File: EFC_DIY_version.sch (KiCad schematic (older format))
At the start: 36 parts, among them J1 Screw_Terminal_01x05, Q1 MJE13005G, Q2 2N3906, Q3 2N3904, U1 NE556

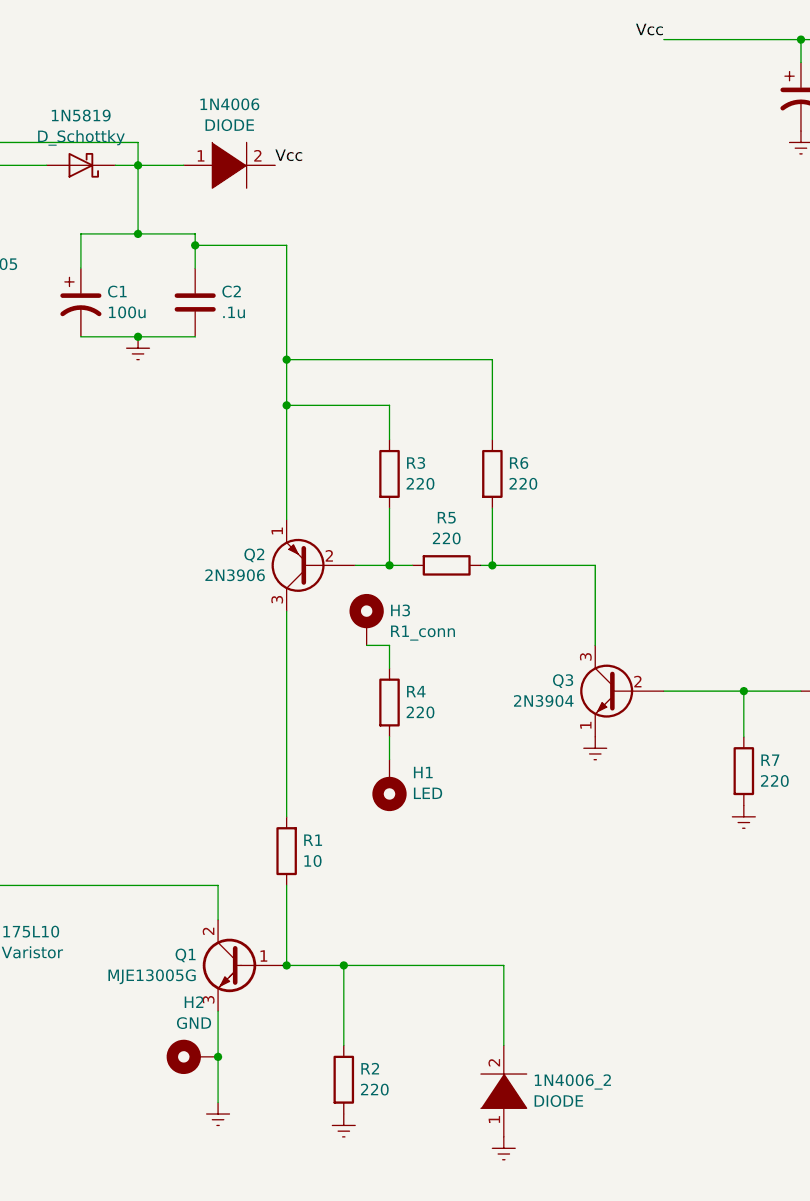
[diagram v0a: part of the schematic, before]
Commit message: Corrected Diode polarity
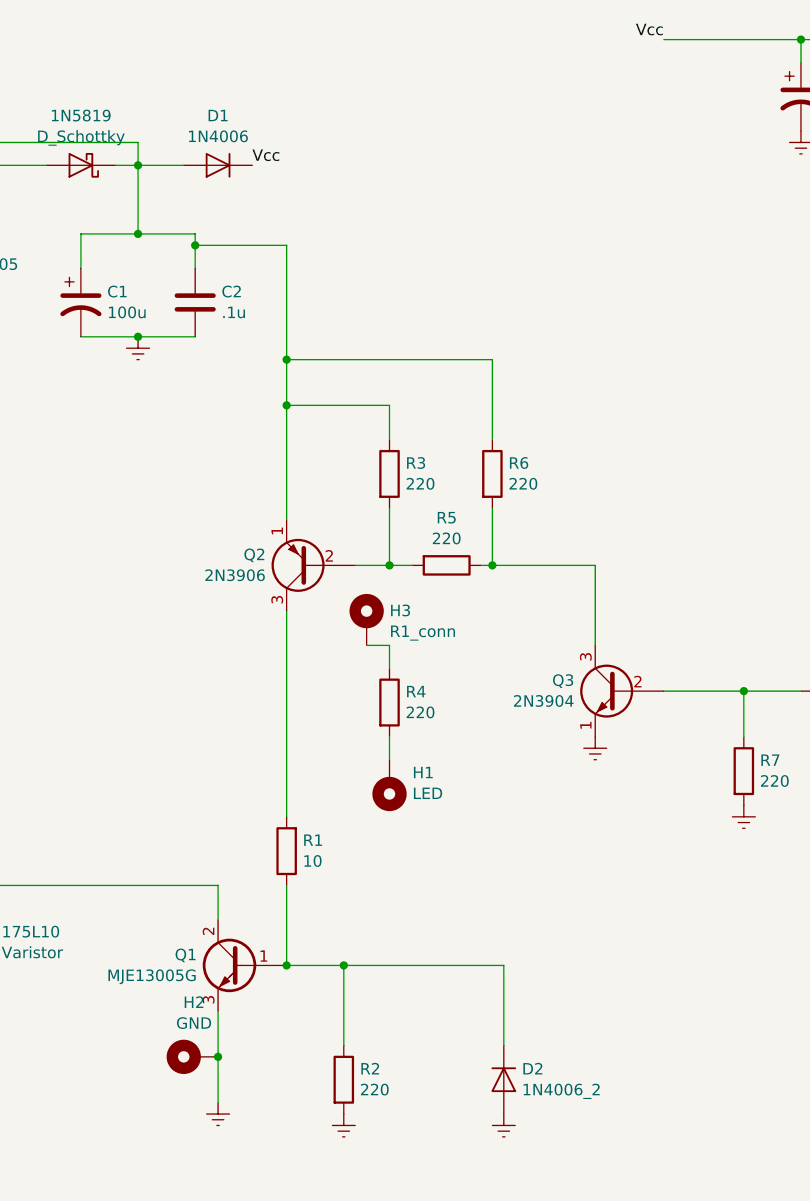
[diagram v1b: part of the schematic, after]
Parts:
- removed 1N4006: DIODE, Diode_SMD:D_2010_5025Metric_Pad1.52x2.65mm_HandSolder, symbol pspice:DIODE
- removed 1N4006_2: DIODE, Diode_THT:D_DO-15_P12.70mm_Horizontal, symbol pspice:DIODE
- added D1: 1N4006, Diode_THT:D_DO-41_SOD81_P10.16mm_Horizontal, symbol Device:D
- added D2: 1N4006_2, Diode_THT:D_DO-41_SOD81_P10.16mm_Horizontal, symbol Device:D
- Q1: footprint digikey-footprints:TO-220-3 -> Package_TO_SOT_THT:TO-220-3_Vertical
- Q2, Q3: footprint digikey-footprints:TO-92-3 -> Package_TO_SOT_THT:TO-92L_Inline_Wide
- U1: footprint Package_DIP:DIP-14_W7.62mm_Socket -> Package_DIP:DIP-14_W7.62mm_Socket_LongPads
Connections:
- net Earth: now also D2.2 (A)
- net Vcc: now also D1.1 (K)
- net at 1N5819.1 (K), C1.1, C2.1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: now also D1.2 (A)
- net at Q1.1 (B), R1.1, R2.1: now also D2.1 (K)
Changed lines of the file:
@@
 EESchema Schematic File Version 4
-LIBS:Fence_Charger-cache
 EELAYER 26 0
 EELAYER END
@@
 $EndComp
 $Comp
-L pspice:DIODE 1N4006
-U 1 1 5E966BEF
-P 2250 1850
-F 0 "1N4006" H 2250 2115 50  0000 C CNN
-F 1 "DIODE" H 2250 2024 50  0000 C CNN
-F 2 "Diode_SMD:D_2010_5025Metric_Pad1.52x2.65mm_HandSolder" H 2250 1850 50  0001 C CNN
-F 3 "~" H 2250 1850 50  0001 C CNN
-	1    2250 1850
-	1    0    0    -1
-$EndComp
-$Comp
 L Device:CP1 C1
 U 1 1 5E966E44
@@
 $EndComp
 $Comp
-L pspice:DIODE 1N4006_2
-U 1 1 5E967028
-P 3450 5900
-F 0 "1N4006_2" V 3496 5772 50  0000 R CNN
-F 1 "DIODE" V 3405 5772 50  0000 R CNN
-F 2 "Diode_THT:D_DO-15_P12.70mm_Horizontal" H 3450 5900 50  0001 C CNN
-F 3 "~" H 3450 5900 50  0001 C CNN
-	1    3450 5900
-	0    -1   -1   0
-$EndComp
-$Comp
 L Transistor_BJT:MJE13005G Q1
 U 1 1 5E96720C
@@
 F 0 "Q1" H 2492 5396 50  0000 L CNN
 F 1 "MJE13005G" H 2492 5305 50  0000 L CNN
-F 2 "digikey-footprints:TO-220-3" H 2550 5275 50  0001 L CIN
+F 2 "Package_TO_SOT_THT:TO-220-3_Vertical" H 2550 5275 50  0001 L CIN
 F 3 "http://www.onsemi.com/pub_link/Collateral/MJE13005-D.PDF" H 2300 5350 50  0001 L CNN
 	1    2300 5350
@@
 L power:Earth #PWR06
 U 1 1 5E967A74
-P 3450 6100
-F 0 "#PWR06" H 3450 5850 50  0001 C CNN
-F 1 "Earth" H 3450 5950 50  0001 C CNN
-F 2 "" H 3450 6100 50  0001 C CNN
-F 3 "~" H 3450 6100 50  0001 C CNN
-	1    3450 6100
+P 3450 6000
+F 0 "#PWR06" H 3450 5750 50  0001 C CNN
+F 1 "Earth" H 3450 5850 50  0001 C CNN
+F 2 "" H 3450 6000 50  0001 C CNN
+F 3 "~" H 3450 6000 50  0001 C CNN
+	1    3450 6000
 	1    0    0    -1
 $EndComp
@@
 F 0 "Q2" H 2791 3554 50  0000 L CNN
 F 1 "2N3906" H 2791 3645 50  0000 L CNN
-F 2 "digikey-footprints:TO-92-3" H 2800 3525 50  0001 L CIN
+F 2 "Package_TO_SOT_THT:TO-92L_Inline_Wide" H 2800 3525 50  0001 L CIN
 F 3 "https://www.fairchildsemi.com/datasheets/2N/2N3906.pdf" H 2600 3600 50  0001 L CNN
 	1    2600 3600
@@
 F 0 "Q3" H 4141 4196 50  0000 L CNN
 F 1 "2N3904" H 4141 4105 50  0000 L CNN
-F 2 "digikey-footprints:TO-92-3" H 4150 4075 50  0001 L CIN
+F 2 "Package_TO_SOT_THT:TO-92L_Inline_Wide" H 4150 4075 50  0001 L CIN
 F 3 "https://www.fairchildsemi.com/datasheets/2N/2N3904.pdf" H 3950 4150 50  0001 L CNN
 	1    3950 4150
@@
 F 0 "U1" H 6250 4928 50  0000 C CNN
 F 1 "NE556" H 6250 4837 50  0000 C CNN
-F 2 "Package_DIP:DIP-14_W7.62mm_Socket" H 6250 4350 50  0001 C CNN
+F 2 "Package_DIP:DIP-14_W7.62mm_Socket_LongPads" H 6250 4350 50  0001 C CNN
 F 3 "http://www.ti.com/lit/ds/symlink/ne556.pdf" H 6250 4350 50  0001 C CNN
 	1    6250 4350
@@
 F 0 "U1" H 8000 4928 50  0000 C CNN
 F 1 "NE556" H 8000 4837 50  0000 C CNN
-F 2 "Package_DIP:DIP-14_W7.62mm_Socket" H 8000 4350 50  0001 C CNN
+F 2 "Package_DIP:DIP-14_W7.62mm_Socket_LongPads" H 8000 4350 50  0001 C CNN
 F 3 "http://www.ti.com/lit/ds/symlink/ne556.pdf" H 8000 4350 50  0001 C CNN
 	2    8000 4350
@@
 Wire Wire Line
 	1850 1750 1850 1850
-Text Label 2450 1850 0    50   ~ 0
+Text Label 2350 1850 0    50   ~ 0
 Vcc
 Text Label 6750 4550 0    50   ~ 0
@@
 Wire Wire Line
 	2500 3800 2500 4700
+$Comp
+L Device:D D1
+U 1 1 5EA2490C
+P 2200 1850
+F 0 "D1" H 2200 1634 50  0000 C CNN
+F 1 "1N4006" H 2200 1725 50  0000 C CNN
+F 2 "Diode_THT:D_DO-41_SOD81_P10.16mm_Horizontal" H 2200 1850 50  0001 C CNN
+F 3 "~" H 2200 1850 50  0001 C CNN
+	1    2200 1850
+	-1   0    0    1
+$EndComp
+$Comp
+L Device:D D2
+U 1 1 5EA24D25
+P 3450 5850
+F 0 "D2" V 3404 5929 50  0000 L CNN
+F 1 "1N4006_2" V 3495 5929 50  0000 L CNN
+F 2 "Diode_THT:D_DO-41_SOD81_P10.16mm_Horizontal" H 3450 5850 50  0001 C CNN
+F 3 "~" H 3450 5850 50  0001 C CNN
+	1    3450 5850
+	0    1    1    0
+$EndComp
 $EndSCHEMATC
